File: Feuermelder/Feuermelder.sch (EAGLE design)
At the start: 9 parts

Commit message: Added some capacitance on VBUS, as per USB spec. 7.2.4.1 / table 7-7 and a bypass capacitor for U1.
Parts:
- removed U$1: TINY25/45/85, avr-7 ulli:TINY25/45/85
- added C1: 4u7, resistor:CPOL-EUE2.5-6
- added C2: 100n, resistor:C-EU050-025X075
- added U1: TINY25/45/85, avr-7 ulli:TINY25/45/85
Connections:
- net N$10: now also U1.(ADC2)PB4; no longer U$1.(ADC2)PB4
- net N$5: now also U1.(AREF)PB0; no longer U$1.(AREF)PB0
- net N$6: now also C1.+, C2.1, U1.VCC; no longer U$1.VCC
- net N$7: now also U1.(OCP)PB1; no longer U$1.(OCP)PB1
- net N$8: now also U1.(ADC3)PB3; no longer U$1.(ADC3)PB3
- net N$9: now also C1.-, C2.2, U1.GND; no longer U$1.GND
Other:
- moved on the sheet: D1, D2, R1, R2, R3, S1, S2, X1
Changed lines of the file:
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@@
 <parts>
 <part name="FRAME1" library="frames" deviceset="DINA5_L" device=""/>
-<part name="U$1" library="avr-7 ulli" deviceset="TINY25/45/85" device=""/>
+<part name="U1" library="avr-7 ulli" deviceset="TINY25/45/85" device=""/>
 <part name="X1" library="con-berg" deviceset="PN61729" device=""/>
 <part name="D1" library="diode" deviceset="1N4004" device=""/>
@@
 <part name="S1" library="switch-omron" deviceset="31-XX" device=""/>
 <part name="S2" library="switch-dil" deviceset="DS01E" device=""/>
+<part name="C1" library="resistor" deviceset="CPOL-EU" device="E2.5-6" value="4u7"/>
+<part name="C2" library="resistor" deviceset="C-EU" device="050-025X075" value="100n"/>
 </parts>
 <sheets>
@@
 <instances>
 <instance part="FRAME1" gate="G$1" x="0" y="0"/>
-<instance part="U$1" gate="G$1" x="139.7" y="86.36" rot="MR0"/>
-<instance part="X1" gate="G$1" x="27.94" y="96.52" rot="MR0"/>
-<instance part="D1" gate="1" x="38.1" y="101.6"/>
-<instance part="D2" gate="1" x="53.34" y="101.6"/>
-<instance part="R1" gate="G$1" x="53.34" y="86.36"/>
-<instance part="R2" gate="G$1" x="53.34" y="78.74"/>
-<instance part="R3" gate="G$1" x="71.12" y="93.98" rot="R90"/>
-<instance part="S1" gate="1" x="109.22" y="66.04"/>
-<instance part="S2" gate="1" x="91.44" y="66.04"/>
+<instance part="U1" gate="G$1" x="137.16" y="83.82" rot="MR0"/>
+<instance part="X1" gate="G$1" x="25.4" y="93.98" rot="MR0"/>
+<instance part="D1" gate="1" x="35.56" y="99.06"/>
+<instance part="D2" gate="1" x="50.8" y="99.06"/>
+<instance part="R1" gate="G$1" x="50.8" y="83.82"/>
+<instance part="R2" gate="G$1" x="50.8" y="76.2"/>
+<instance part="R3" gate="G$1" x="68.58" y="91.44" rot="R90"/>
+<instance part="S1" gate="1" x="106.68" y="63.5"/>
+<instance part="S2" gate="1" x="88.9" y="63.5"/>
+<instance part="C1" gate="G$1" x="73.66" y="63.5"/>
+<instance part="C2" gate="G$1" x="165.1" y="81.28"/>
 </instances>
 <busses>
@@
 <pinref part="X1" gate="G$1" pin="1"/>
 <pinref part="D1" gate="1" pin="A"/>
-<wire x1="30.48" y1="101.6" x2="35.56" y2="101.6" width="0.1524" layer="91"/>
+<wire x1="27.94" y1="99.06" x2="33.02" y2="99.06" width="0.1524" layer="91"/>
 </segment>
 </net>
@@
 <pinref part="D1" gate="1" pin="C"/>
 <pinref part="D2" gate="1" pin="A"/>
-<wire x1="40.64" y1="101.6" x2="50.8" y2="101.6" width="0.1524" layer="91"/>
+<wire x1="38.1" y1="99.06" x2="48.26" y2="99.06" width="0.1524" layer="91"/>
 </segment>
 </net>
@@
 <segment>
 <pinref part="R1" gate="G$1" pin="1"/>
-<wire x1="48.26" y1="86.36" x2="43.18" y2="86.36" width="0.1524" layer="91"/>
+<wire x1="45.72" y1="83.82" x2="40.64" y2="83.82" width="0.1524" layer="91"/>
 <pinref part="X1" gate="G$1" pin="2"/>
-<wire x1="43.18" y1="86.36" x2="43.18" y2="99.06" width="0.1524" layer="91"/>
-<wire x1="43.18" y1="99.06" x2="30.48" y2="99.06" width="0.1524" layer="91"/>
+<wire x1="40.64" y1="83.82" x2="40.64" y2="96.52" width="0.1524" layer="91"/>
+<wire x1="40.64" y1="96.52" x2="27.94" y2="96.52" width="0.1524" layer="91"/>
 </segment>
 </net>
@@
 <segment>
 <pinref part="X1" gate="G$1" pin="3"/>
-<wire x1="30.48" y1="96.52" x2="38.1" y2="96.52" width="0.1524" layer="91"/>
-<wire x1="38.1" y1="96.52" x2="38.1" y2="78.74" width="0.1524" layer="91"/>
+<wire x1="27.94" y1="93.98" x2="35.56" y2="93.98" width="0.1524" layer="91"/>
+<wire x1="35.56" y1="93.98" x2="35.56" y2="76.2" width="0.1524" layer="91"/>
 <pinref part="R2" gate="G$1" pin="1"/>
-<wire x1="38.1" y1="78.74" x2="48.26" y2="78.74" width="0.1524" layer="91"/>
+<wire x1="35.56" y1="76.2" x2="45.72" y2="76.2" width="0.1524" layer="91"/>
 </segment>
 </net>
@@
 <segment>
 <pinref part="R1" gate="G$1" pin="2"/>
-<wire x1="58.42" y1="86.36" x2="71.12" y2="86.36" width="0.1524" layer="91"/>
+<wire x1="55.88" y1="83.82" x2="68.58" y2="83.82" width="0.1524" layer="91"/>
 <pinref part="R3" gate="G$1" pin="1"/>
-<wire x1="71.12" y1="86.36" x2="71.12" y2="88.9" width="0.1524" layer="91"/>
-<wire x1="71.12" y1="86.36" x2="71.12" y2="81.28" width="0.1524" layer="91"/>
-<wire x1="71.12" y1="81.28" x2="121.92" y2="81.28" width="0.1524" layer="91"/>
-<junction x="71.12" y="86.36"/>
-<pinref part="U$1" gate="G$1" pin="(AREF)PB0"/>
+<wire x1="68.58" y1="83.82" x2="68.58" y2="86.36" width="0.1524" layer="91"/>
+<wire x1="68.58" y1="83.82" x2="68.58" y2="78.74" width="0.1524" layer="91"/>
+<wire x1="68.58" y1="78.74" x2="119.38" y2="78.74" width="0.1524" layer="91"/>
+<junction x="68.58" y="83.82"/>
+<pinref part="U1" gate="G$1" pin="(AREF)PB0"/>
 </segment>
 </net>
@@
 <segment>
 <pinref part="R3" gate="G$1" pin="2"/>
-<wire x1="71.12" y1="99.06" x2="71.12" y2="101.6" width="0.1524" layer="91"/>
-<wire x1="71.12" y1="101.6" x2="55.88" y2="101.6" width="0.1524" layer="91"/>
+<wire x1="68.58" y1="96.52" x2="68.58" y2="99.06" width="0.1524" layer="91"/>
+<wire x1="68.58" y1="99.06" x2="53.34" y2="99.06" width="0.1524" layer="91"/>
 <pinref part="D2" gate="1" pin="C"/>
-<junction x="71.12" y="101.6"/>
-<wire x1="71.12" y1="101.6" x2="162.56" y2="101.6" width="0.1524" layer="91"/>
-<wire x1="162.56" y1="101.6" x2="162.56" y2="83.82" width="0.1524" layer="91"/>
-<pinref part="U$1" gate="G$1" pin="VCC"/>
-<wire x1="162.56" y1="83.82" x2="157.48" y2="83.82" width="0.1524" layer="91"/>
+<junction x="68.58" y="99.06"/>
+<wire x1="68.58" y1="99.06" x2="73.66" y2="99.06" width="0.1524" layer="91"/>
+<wire x1="73.66" y1="99.06" x2="160.02" y2="99.06" width="0.1524" layer="91"/>
+<wire x1="160.02" y1="99.06" x2="160.02" y2="81.28" width="0.1524" layer="91"/>
+<pinref part="U1" gate="G$1" pin="VCC"/>
+<wire x1="160.02" y1="81.28" x2="154.94" y2="81.28" width="0.1524" layer="91"/>
+<pinref part="C1" gate="G$1" pin="+"/>
+<wire x1="73.66" y1="66.04" x2="73.66" y2="99.06" width="0.1524" layer="91"/>
+<junction x="73.66" y="99.06"/>
+<pinref part="C2" gate="G$1" pin="1"/>
+<wire x1="165.1" y1="83.82" x2="165.1" y2="99.06" width="0.1524" layer="91"/>
+<wire x1="165.1" y1="99.06" x2="160.02" y2="99.06" width="0.1524" layer="91"/>
+<junction x="160.02" y="99.06"/>
 </segment>
 </net>
@@
 <segment>
 <pinref part="R2" gate="G$1" pin="2"/>
-<wire x1="58.42" y1="78.74" x2="116.84" y2="78.74" width="0.1524" layer="91"/>
-<wire x1="116.84" y1="78.74" x2="116.84" y2="83.82" width="0.1524" layer="91"/>
-<pinref part="U$1" gate="G$1" pin="(OCP)PB1"/>
-<wire x1="116.84" y1="83.82" x2="121.92" y2="83.82" width="0.1524" layer="91"/>
+<wire x1="55.88" y1="76.2" x2="114.3" y2="76.2" width="0.1524" layer="91"/>
+<wire x1="114.3" y1="76.2" x2="114.3" y2="81.28" width="0.1524" layer="91"/>
+<pinref part="U1" gate="G$1" pin="(OCP)PB1"/>
+<wire x1="114.3" y1="81.28" x2="119.38" y2="81.28" width="0.1524" layer="91"/>
 </segment>
 </net>
@@
 <segment>
 <pinref part="X1" gate="G$1" pin="4"/>
-<wire x1="30.48" y1="93.98" x2="33.02" y2="93.98" width="0.1524" layer="91"/>
-<wire x1="33.02" y1="93.98" x2="33.02" y2="55.88" width="0.1524" layer="91"/>
-<wire x1="33.02" y1="55.88" x2="91.44" y2="55.88" width="0.1524" layer="91"/>
-<pinref part="U$1" gate="G$1" pin="GND"/>
-<wire x1="91.44" y1="55.88" x2="109.22" y2="55.88" width="0.1524" layer="91"/>
-<wire x1="109.22" y1="55.88" x2="162.56" y2="55.88" width="0.1524" layer="91"/>
-<wire x1="162.56" y1="55.88" x2="162.56" y2="81.28" width="0.1524" layer="91"/>
-<wire x1="162.56" y1="81.28" x2="157.48" y2="81.28" width="0.1524" layer="91"/>
+<wire x1="27.94" y1="91.44" x2="30.48" y2="91.44" width="0.1524" layer="91"/>
+<wire x1="30.48" y1="91.44" x2="30.48" y2="53.34" width="0.1524" layer="91"/>
+<wire x1="30.48" y1="53.34" x2="73.66" y2="53.34" width="0.1524" layer="91"/>
+<pinref part="U1" gate="G$1" pin="GND"/>
+<wire x1="73.66" y1="53.34" x2="88.9" y2="53.34" width="0.1524" layer="91"/>
+<wire x1="88.9" y1="53.34" x2="106.68" y2="53.34" width="0.1524" layer="91"/>
+<wire x1="106.68" y1="53.34" x2="160.02" y2="53.34" width="0.1524" layer="91"/>
+<wire x1="160.02" y1="53.34" x2="160.02" y2="78.74" width="0.1524" layer="91"/>
+<wire x1="160.02" y1="78.74" x2="154.94" y2="78.74" width="0.1524" layer="91"/>
 <pinref part="S1" gate="1" pin="P"/>
-<wire x1="109.22" y1="60.96" x2="109.22" y2="55.88" width="0.1524" layer="91"/>
-<junction x="109.22" y="55.88"/>
+<wire x1="106.68" y1="58.42" x2="106.68" y2="53.34" width="0.1524" layer="91"/>
+<junction x="106.68" y="53.34"/>
 <pinref part="S2" gate="1" pin="1"/>
-<wire x1="91.44" y1="60.96" x2="91.44" y2="55.88" width="0.1524" layer="91"/>
-<junction x="91.44" y="55.88"/>
+<wire x1="88.9" y1="58.42" x2="88.9" y2="53.34" width="0.1524" layer="91"/>
+<junction x="88.9" y="53.34"/>
+<pinref part="C1" gate="G$1" pin="-"/>
+<wire x1="73.66" y1="58.42" x2="73.66" y2="53.34" width="0.1524" layer="91"/>
+<junction x="73.66" y="53.34"/>
+<pinref part="C2" gate="G$1" pin="2"/>
+<wire x1="165.1" y1="76.2" x2="165.1" y2="53.34" width="0.1524" layer="91"/>
+<wire x1="165.1" y1="53.34" x2="160.02" y2="53.34" width="0.1524" layer="91"/>
+<junction x="160.02" y="53.34"/>
 </segment>
 </net>
 <net name="N$10" class="0">
 <segment>
-<pinref part="U$1" gate="G$1" pin="(ADC2)PB4"/>
+<pinref part="U1" gate="G$1" pin="(ADC2)PB4"/>
 <pinref part="S2" gate="1" pin="2"/>
-<wire x1="121.92" y1="91.44" x2="91.44" y2="91.44" width="0.1524" layer="91"/>
-<wire x1="91.44" y1="91.44" x2="91.44" y2="71.12" width="0.1524" layer="91"/>
+<wire x1="119.38" y1="88.9" x2="88.9" y2="88.9" width="0.1524" layer="91"/>
+<wire x1="88.9" y1="88.9" x2="88.9" y2="68.58" width="0.1524" layer="91"/>
 </segment>
 </net>
 <net name="N$8" class="0">
 <segment>
-<pinref part="U$1" gate="G$1" pin="(ADC3)PB3"/>
+<pinref part="U1" gate="G$1" pin="(ADC3)PB3"/>
 <pinref part="S1" gate="1" pin="S"/>
-<wire x1="121.92" y1="88.9" x2="109.22" y2="88.9" width="0.1524" layer="91"/>
-<wire x1="109.22" y1="88.9" x2="109.22" y2="71.12" width="0.1524" layer="91"/>
+<wire x1="119.38" y1="86.36" x2="106.68" y2="86.36" width="0.1524" layer="91"/>
+<wire x1="106.68" y1="86.36" x2="106.68" y2="68.58" width="0.1524" layer="91"/>
 </segment>
 </net>

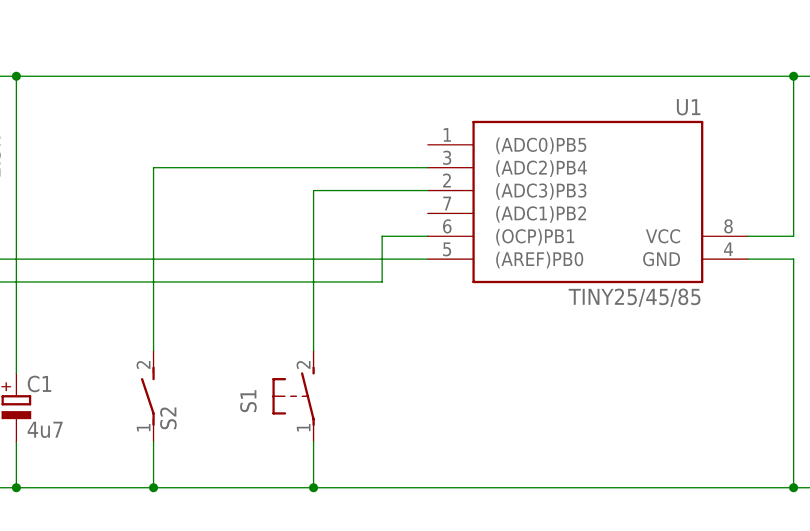
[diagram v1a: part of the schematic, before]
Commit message: Bugfix: USB D- was wrongly connected to PB1 instead of PB2.
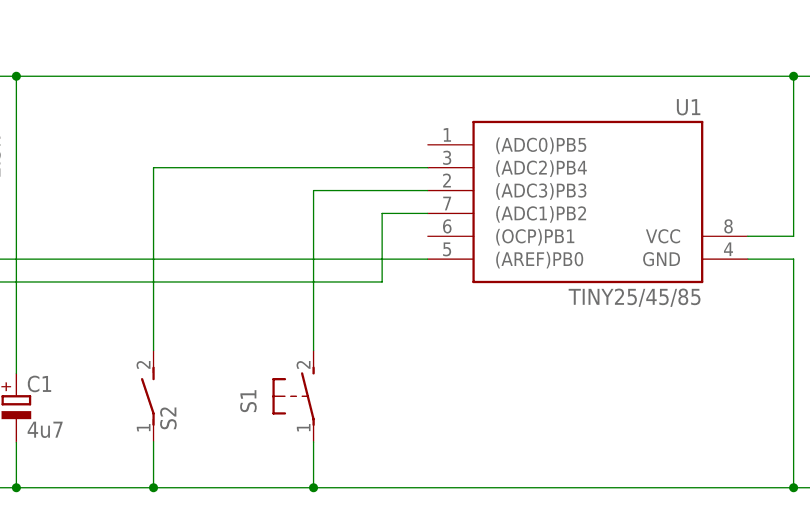
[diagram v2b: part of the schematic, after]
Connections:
- net N$1 renamed USB_D-
- net N$2 renamed USB_VCC
- net N$4 renamed USB_D+
- net N$6 renamed 3V6
- net N$9 renamed USB_GND
- net N$7: now also U1.(ADC1)PB2; no longer U1.(OCP)PB1
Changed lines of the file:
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@@
 </busses>
 <nets>
-<net name="N$2" class="0">
+<net name="USB_VCC" class="0">
 <segment>
 <pinref part="X1" gate="G$1" pin="1"/>
@@
 </segment>
 </net>
-<net name="N$1" class="0">
+<net name="USB_D-" class="0">
 <segment>
 <pinref part="R1" gate="G$1" pin="1"/>
@@
 </segment>
 </net>
-<net name="N$4" class="0">
+<net name="USB_D+" class="0">
 <segment>
 <pinref part="X1" gate="G$1" pin="3"/>
@@
 </segment>
 </net>
-<net name="N$6" class="0">
+<net name="3V6" class="0">
 <segment>
 <pinref part="R3" gate="G$1" pin="2"/>
@@
 <pinref part="R2" gate="G$1" pin="2"/>
 <wire x1="55.88" y1="76.2" x2="114.3" y2="76.2" width="0.1524" layer="91"/>
-<wire x1="114.3" y1="76.2" x2="114.3" y2="81.28" width="0.1524" layer="91"/>
-<pinref part="U1" gate="G$1" pin="(OCP)PB1"/>
-<wire x1="114.3" y1="81.28" x2="119.38" y2="81.28" width="0.1524" layer="91"/>
+<wire x1="114.3" y1="76.2" x2="114.3" y2="83.82" width="0.1524" layer="91"/>
+<pinref part="U1" gate="G$1" pin="(ADC1)PB2"/>
+<wire x1="114.3" y1="83.82" x2="119.38" y2="83.82" width="0.1524" layer="91"/>
 </segment>
 </net>
-<net name="N$9" class="0">
+<net name="USB_GND" class="0">
 <segment>
 <pinref part="X1" gate="G$1" pin="4"/>
